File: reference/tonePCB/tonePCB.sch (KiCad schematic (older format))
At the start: 13 parts, among them J1 to_ftdi, U1 ATMEGA328P-PU

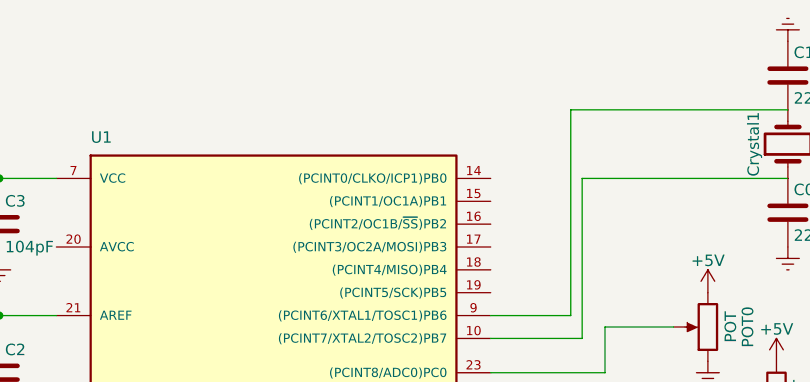
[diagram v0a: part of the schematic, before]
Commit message: Adding an LED to the project
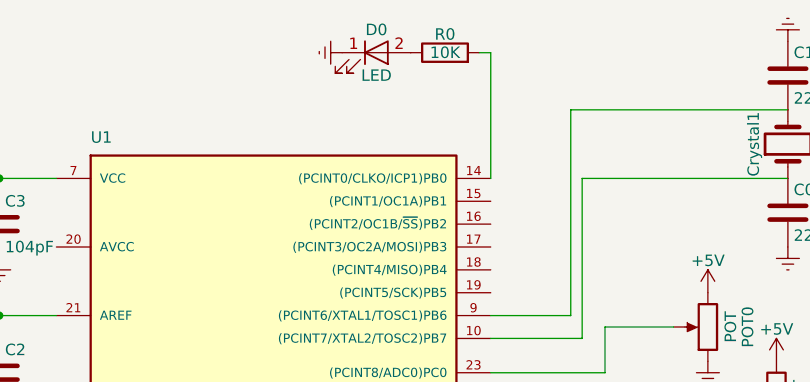
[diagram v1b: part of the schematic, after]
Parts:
- added D0: LED, LEDs:LED_D3.0mm_FlatTop, symbol LED
- added R0: 10K, Resistors_THT:R_Axial_DIN0204_L3.6mm_D1.6mm_P5.08mm_Horizontal, symbol R
- C0, C1, C2, C3: footprint Capacitors_THT:C_Rect_L9.0mm_W2.5mm_P7.50mm_MKT -> Capacitors_THT:C_Rect_L4.0mm_W2.5mm_P2.50mm
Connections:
- net Earth: now also D0.1 (K)
- net at U1.14 ((PCINT0/CLKO/ICP1)PB0): now also R0.2
- new net: D0.2 (A), R0.1
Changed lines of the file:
@@
 $EndDescr
 $Comp
-L Earth #PWR4
+L Earth #PWR01
 U 1 1 58F529D4
 P 4050 5900
-F 0 "#PWR4" H 4050 5650 50  0001 C CNN
+F 0 "#PWR01" H 4050 5650 50  0001 C CNN
 F 1 "Earth" H 4050 5750 50  0001 C CNN
 F 2 "" H 4050 5900 50  0001 C CNN
@@
 $EndComp
 $Comp
-L +5V #PWR1
+L +5V #PWR02
 U 1 1 58F529EF
 P 3800 3700
-F 0 "#PWR1" H 3800 3550 50  0001 C CNN
+F 0 "#PWR02" H 3800 3550 50  0001 C CNN
 F 1 "+5V" H 3800 3840 50  0000 C CNN
 F 2 "" H 3800 3700 50  0001 C CNN
@@
 $EndComp
 $Comp
-L +5V #PWR7
+L +5V #PWR03
 U 1 1 58F61F9C
 P 7050 4200
-F 0 "#PWR7" H 7050 4050 50  0001 C CNN
+F 0 "#PWR03" H 7050 4050 50  0001 C CNN
 F 1 "+5V" H 7050 4340 50  0000 C CNN
 F 2 "" H 7050 4200 50  0001 C CNN
@@
 $EndComp
 $Comp
-L Earth #PWR8
+L Earth #PWR04
 U 1 1 58F61FC8
 P 7050 4500
-F 0 "#PWR8" H 7050 4250 50  0001 C CNN
+F 0 "#PWR04" H 7050 4250 50  0001 C CNN
 F 1 "Earth" H 7050 4350 50  0001 C CNN
 F 2 "" H 7050 4500 50  0001 C CNN
@@
 $EndComp
 $Comp
-L +5V #PWR13
+L +5V #PWR05
 U 1 1 58F62057
 P 7350 4500
-F 0 "#PWR13" H 7350 4350 50  0001 C CNN
+F 0 "#PWR05" H 7350 4350 50  0001 C CNN
 F 1 "+5V" H 7350 4640 50  0000 C CNN
 F 2 "" H 7350 4500 50  0001 C CNN
@@
 $EndComp
 $Comp
-L Earth #PWR14
+L Earth #PWR06
 U 1 1 58F6205D
 P 7350 4800
-F 0 "#PWR14" H 7350 4550 50  0001 C CNN
+F 0 "#PWR06" H 7350 4550 50  0001 C CNN
 F 1 "Earth" H 7350 4650 50  0001 C CNN
 F 2 "" H 7350 4800 50  0001 C CNN
@@
 $EndComp
 $Comp
-L +5V #PWR9
+L +5V #PWR07
 U 1 1 58F620A0
 P 7050 4850
-F 0 "#PWR9" H 7050 4700 50  0001 C CNN
+F 0 "#PWR07" H 7050 4700 50  0001 C CNN
 F 1 "+5V" H 7050 4990 50  0000 C CNN
 F 2 "" H 7050 4850 50  0001 C CNN
@@
 $EndComp
 $Comp
-L Earth #PWR10
+L Earth #PWR08
 U 1 1 58F620A6
 P 7050 5150
-F 0 "#PWR10" H 7050 4900 50  0001 C CNN
+F 0 "#PWR08" H 7050 4900 50  0001 C CNN
 F 1 "Earth" H 7050 5000 50  0001 C CNN
 F 2 "" H 7050 5150 50  0001 C CNN
@@
 $EndComp
 $Comp
-L +5V #PWR15
+L +5V #PWR09
 U 1 1 58F625C2
 P 7350 5150
-F 0 "#PWR15" H 7350 5000 50  0001 C CNN
+F 0 "#PWR09" H 7350 5000 50  0001 C CNN
 F 1 "+5V" H 7350 5290 50  0000 C CNN
 F 2 "" H 7350 5150 50  0001 C CNN
@@
 $EndComp
 $Comp
-L Earth #PWR16
+L Earth #PWR010
 U 1 1 58F625C8
 P 7350 5450
-F 0 "#PWR16" H 7350 5200 50  0001 C CNN
+F 0 "#PWR010" H 7350 5200 50  0001 C CNN
 F 1 "Earth" H 7350 5300 50  0001 C CNN
 F 2 "" H 7350 5450 50  0001 C CNN
@@
 $EndComp
 $Comp
-L +5V #PWR11
+L +5V #PWR011
 U 1 1 58F62656
 P 7050 5500
-F 0 "#PWR11" H 7050 5350 50  0001 C CNN
+F 0 "#PWR011" H 7050 5350 50  0001 C CNN
 F 1 "+5V" H 7050 5640 50  0000 C CNN
 F 2 "" H 7050 5500 50  0001 C CNN
@@
 $EndComp
 $Comp
-L Earth #PWR12
+L Earth #PWR012
 U 1 1 58F6265C
 P 7050 5800
-F 0 "#PWR12" H 7050 5550 50  0001 C CNN
+F 0 "#PWR012" H 7050 5550 50  0001 C CNN
 F 1 "Earth" H 7050 5650 50  0001 C CNN
 F 2 "" H 7050 5800 50  0001 C CNN
@@
 $EndComp
 $Comp
-L +5V #PWR17
+L +5V #PWR013
 U 1 1 58F626B6
 P 7350 5800
-F 0 "#PWR17" H 7350 5650 50  0001 C CNN
+F 0 "#PWR013" H 7350 5650 50  0001 C CNN
 F 1 "+5V" H 7350 5940 50  0000 C CNN
 F 2 "" H 7350 5800 50  0001 C CNN
@@
 $EndComp
 $Comp
-L Earth #PWR18
+L Earth #PWR014
 U 1 1 58F626BC
 P 7350 6100
-F 0 "#PWR18" H 7350 5850 50  0001 C CNN
+F 0 "#PWR014" H 7350 5850 50  0001 C CNN
 F 1 "Earth" H 7350 5950 50  0001 C CNN
 F 2 "" H 7350 6100 50  0001 C CNN
@@
 F 0 "C2" H 3975 4650 50  0000 L CNN
 F 1 "104uF" H 3975 4450 50  0000 L CNN
-F 2 "Capacitors_THT:C_Rect_L9.0mm_W2.5mm_P7.50mm_MKT" H 3988 4400 50  0001 C CNN
+F 2 "Capacitors_THT:C_Rect_L4.0mm_W2.5mm_P2.50mm" H 3988 4400 50  0001 C CNN
 F 3 "" H 3950 4550 50  0001 C CNN
 	1    3950 4550
@@
 F 0 "C3" H 3975 4000 50  0000 L CNN
 F 1 "104pF" H 3975 3800 50  0000 L CNN
-F 2 "Capacitors_THT:C_Rect_L9.0mm_W2.5mm_P7.50mm_MKT" H 3988 3750 50  0001 C CNN
+F 2 "Capacitors_THT:C_Rect_L4.0mm_W2.5mm_P2.50mm" H 3988 3750 50  0001 C CNN
 F 3 "" H 3950 3900 50  0001 C CNN
 	1    3950 3900
@@
 $EndComp
 $Comp
-L Earth #PWR3
+L Earth #PWR015
 U 1 1 58F62A4A
 P 3950 4700
-F 0 "#PWR3" H 3950 4450 50  0001 C CNN
+F 0 "#PWR015" H 3950 4450 50  0001 C CNN
 F 1 "Earth" H 3950 4550 50  0001 C CNN
 F 2 "" H 3950 4700 50  0001 C CNN
@@
 F 0 "C0" H 7425 3950 50  0000 L CNN
 F 1 "22uF" H 7425 3750 50  0000 L CNN
-F 2 "Capacitors_THT:C_Rect_L9.0mm_W2.5mm_P7.50mm_MKT" H 7438 3700 50  0001 C CNN
+F 2 "Capacitors_THT:C_Rect_L4.0mm_W2.5mm_P2.50mm" H 7438 3700 50  0001 C CNN
 F 3 "" H 7400 3850 50  0001 C CNN
 	1    7400 3850
@@
 F 0 "C1" H 7425 3350 50  0000 L CNN
 F 1 "22uF" H 7425 3150 50  0000 L CNN
-F 2 "Capacitors_THT:C_Rect_L9.0mm_W2.5mm_P7.50mm_MKT" H 7438 3100 50  0001 C CNN
+F 2 "Capacitors_THT:C_Rect_L4.0mm_W2.5mm_P2.50mm" H 7438 3100 50  0001 C CNN
 F 3 "" H 7400 3250 50  0001 C CNN
 	1    7400 3250
@@
 $EndComp
 $Comp
-L Earth #PWR20
+L Earth #PWR016
 U 1 1 58F62C7C
 P 7400 4000
-F 0 "#PWR20" H 7400 3750 50  0001 C CNN
+F 0 "#PWR016" H 7400 3750 50  0001 C CNN
 F 1 "Earth" H 7400 3850 50  0001 C CNN
 F 2 "" H 7400 4000 50  0001 C CNN
@@
 $EndComp
 $Comp
-L Earth #PWR19
+L Earth #PWR017
 U 1 1 58F62CB4
 P 7400 3100
-F 0 "#PWR19" H 7400 2850 50  0001 C CNN
+F 0 "#PWR017" H 7400 2850 50  0001 C CNN
 F 1 "Earth" H 7400 2950 50  0001 C CNN
 F 2 "" H 7400 3100 50  0001 C CNN
@@
 $EndComp
 $Comp
-L Earth #PWR2
+L Earth #PWR018
 U 1 1 58F62A06
 P 3950 4050
-F 0 "#PWR2" H 3950 3800 50  0001 C CNN
+F 0 "#PWR018" H 3950 3800 50  0001 C CNN
 F 1 "Earth" H 3950 3900 50  0001 C CNN
 F 2 "" H 3950 4050 50  0001 C CNN
@@
 $EndComp
 $Comp
-L Earth #PWR6
+L Earth #PWR019
 U 1 1 58F6AA72
 P 6800 6200
-F 0 "#PWR6" H 6800 5950 50  0001 C CNN
+F 0 "#PWR019" H 6800 5950 50  0001 C CNN
 F 1 "Earth" H 6800 6050 50  0001 C CNN
 F 2 "" H 6800 6200 50  0001 C CNN
@@
 $EndComp
 $Comp
-L +5V #PWR5
+L +5V #PWR020
 U 1 1 58F6AAAD
 P 6800 6100
-F 0 "#PWR5" H 6800 5950 50  0001 C CNN
+F 0 "#PWR020" H 6800 5950 50  0001 C CNN
 F 1 "+5V" H 6800 6240 50  0000 C CNN
 F 2 "" H 6800 6100 50  0001 C CNN
@@
 Wire Wire Line
 	6300 5400 6100 5400
+$Comp
+L LED D0
+U 1 1 58FB7A0E
+P 5600 3150
+F 0 "D0" H 5600 3250 50  0000 C CNN
+F 1 "LED" H 5600 3050 50  0000 C CNN
+F 2 "LEDs:LED_D3.0mm_FlatTop" H 5600 3150 50  0001 C CNN
+F 3 "" H 5600 3150 50  0001 C CNN
+	1    5600 3150
+	1    0    0    -1
+$EndComp
+$Comp
+L R R0
+U 1 1 58FB7A78
+P 5900 3150
+F 0 "R0" V 5980 3150 50  0000 C CNN
+F 1 "10K" V 5900 3150 50  0000 C CNN
+F 2 "Resistors_THT:R_Axial_DIN0204_L3.6mm_D1.6mm_P5.08mm_Horizontal" V 5830 3150 50  0001 C CNN
+F 3 "" H 5900 3150 50  0001 C CNN
+	1    5900 3150
+	0    -1   -1   0
+$EndComp
+Wire Wire Line
+	6050 3150 6100 3150
+Wire Wire Line
+	6100 3150 6100 3700
+$Comp
+L Earth #PWR021
+U 1 1 58FB7B18
+P 5450 3150
+F 0 "#PWR021" H 5450 2900 50  0001 C CNN
+F 1 "Earth" H 5450 3000 50  0001 C CNN
+F 2 "" H 5450 3150 50  0001 C CNN
+F 3 "" H 5450 3150 50  0001 C CNN
+	1    5450 3150
+	0    1    1    0
+$EndComp
 $EndSCHEMATC
